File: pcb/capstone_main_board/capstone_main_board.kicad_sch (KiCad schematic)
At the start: 46 parts, among them J1 Vin, J10 MOSI, J11 SCLK, J12 NCS, J13 Vin, J18 SDO, J19 BAT, J2 VDD OS, J20 IO14, J21 IO13, J22 IO10, J23 IO8, J24 IO6, J25 RX0, J26 TX0, J27 D+, J28 D-, J29 100, J3 VDDA, J30 5V, J31 RESET, J32 Vin, J4 MFIO, J5 VDD FS, J6 V2, J7 V1, J8 Motion, J9 MISO, Q1 BSS138, Q2 BSS138, U1 OMGS3, U2 ADXL345, U3 TPS73219DBVT, U5 VREG_SOT23-5

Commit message: sensor and mcu board nearly complete
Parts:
- removed C2, C4: 1uF, Library:CAP_CL10_SAM, symbol Device:C
- removed C7: 10µF, Library:CAP_CL21_SAM, symbol Adafruit ADXL345 Triple-Axis Accelerometer-eagle-import:CAP_CERAMIC0805-NOOUTLI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
- removed C8: 0.1uF, Library:CAP_CL05_SAM, symbol Adafruit ADXL345 Triple-Axis Accelerometer-eagle-import:CAP_CERAMIC0805-NOOUTLI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
- removed D1: 1N4148, Library:SOD3715X135N, symbol Adafruit ADXL345 Triple-Axis Accelerometer-eagle-import:microbuilder_DIODE_SOD3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
- removed J1, J13, J32: Vin, Connector_PinHeader_1.00mm:PinHeader_1x01_P1.00mm_Vertical, symbol Connector:Conn_01x01_Pin
- removed J18: SDO, Connector_PinHeader_1.00mm:PinHeader_1x01_P1.00mm_Vertical, symbol Connector:Conn_01x01_Pin
- removed J2: VDD OS, Connector_PinHeader_1.00mm:PinHeader_1x01_P1.00mm_Vertical, symbol Connector:Conn_01x01_Pin
- removed J20: IO14, Connector_PinHeader_1.00mm:PinHeader_1x01_P1.00mm_Vertical, symbol Connector:Conn_01x01_Pin
- removed J21: IO13, Connector_PinHeader_1.00mm:PinHeader_1x01_P1.00mm_Vertical, symbol Connector:Conn_01x01_Pin
- removed J22: IO10, Connector_PinHeader_1.00mm:PinHeader_1x01_P1.00mm_Vertical, symbol Connector:Conn_01x01_Pin
- removed J23: IO8, Connector_PinHeader_1.00mm:PinHeader_1x01_P1.00mm_Vertical, symbol Connector:Conn_01x01_Pin
- removed J24: IO6, Connector_PinHeader_1.00mm:PinHeader_1x01_P1.00mm_Vertical, symbol Connector:Conn_01x01_Pin
- removed J25: RX0, Connector_PinHeader_1.00mm:PinHeader_1x01_P1.00mm_Vertical, symbol Connector:Conn_01x01_Pin
- removed J26: TX0, Connector_PinHeader_1.00mm:PinHeader_1x01_P1.00mm_Vertical, symbol Connector:Conn_01x01_Pin
- removed J27: D+, Connector_PinHeader_1.00mm:PinHeader_1x01_P1.00mm_Vertical, symbol Connector:Conn_01x01_Pin
- removed J28: D-, Connector_PinHeader_1.00mm:PinHeader_1x01_P1.00mm_Vertical, symbol Connector:Conn_01x01_Pin
- removed J29: 100, Connector_PinHeader_1.00mm:PinHeader_1x01_P1.00mm_Vertical, symbol Connector:Conn_01x01_Pin
- removed J30: 5V, Connector_PinHeader_1.00mm:PinHeader_1x01_P1.00mm_Vertical, symbol Connector:Conn_01x01_Pin
- removed J31: RESET, Connector_PinHeader_1.00mm:PinHeader_1x01_P1.00mm_Vertical, symbol Connector:Conn_01x01_Pin
- removed J5: VDD FS, Connector_PinHeader_1.00mm:PinHeader_1x01_P1.00mm_Vertical, symbol Connector:Conn_01x01_Pin
- removed Q1, Q2: BSS138, Library:SOT95P240X111-3N, symbol Adafruit ADXL345 Triple-Axis Accelerometer-eagle-import:MOSFET-NWIDE
- removed R4, R5, R6, R7: 10K, Library:RES_ERJ2RKF1002X, symbol Adafruit ADXL345 Triple-Axis Accelerometer-eagle-import:RESISTOR0805_NOOUTLINE
- removed U1: OMGS3, Library:OMGS3, symbol New_Library:OMGS3
- removed U2: ADXL345, Library:PQFN80P500X300X100-14N, symbol New_Library:ADXL345
- removed U3: TPS73219DBVT, Library:DBV5_TEX, symbol New_Library:TPS73219DBVT
- added C1: 10uF, Capacitor_SMD:C_0805_2012Metric, symbol Device:C
- added C3: 0.1uF, Capacitor_SMD:C_0402_1005Metric, symbol Device:C
- added C5: 1uF, Capacitor_SMD:C_0603_1608Metric, symbol Device:C
- added J7: VBAT-, Connector_PinHeader_2.00mm:PinHeader_1x01_P2.00mm_Vertical, symbol Connector:Conn_01x01_Pin
- added J8: Conn_01x07_Pin, Custom_FP:OMGS3_programming_pins, symbol Connector:Conn_01x07_Pin
- added R2: 10k, Resistor_SMD:R_0402_1005Metric, symbol Device:R
- added U1: OMGS3, Imported_FP:OMGS3, symbol Imported_sym:OMGS3
- added U3: ADXL345, Imported_FP:PQFN80P500X300X100-14N, symbol Imported_sym:ADXL345
- added U4: TPS73219DBVT, Imported_FP:DBV5_TEX, symbol Custom_sym:TPS73219DBVT
- C2: renamed from C1; footprint Library:CAP_CL10_SAM -> Capacitor_SMD:C_0603_1608Metric
- C4: renamed from C3; footprint Library:CAP_CL10_SAM -> Capacitor_SMD:C_0603_1608Metric
- J1: renamed from J4; footprint Connector_PinHeader_1.00mm:PinHeader_1x01_P1.00mm_Vertical -> Connector_PinHeader_2.00mm:PinHeader_1x01_P2.00mm_Vertical
- J10: renamed from J7; value V1 -> FORCE_V1; footprint Connector_PinHeader_1.00mm:PinHeader_1x01_P1.00mm_Vertical -> Connector_PinHeader_2.00mm:PinHeader_1x01_P2.00mm_Vertical
- J11: renamed from J19; value BAT -> VBAT+; footprint Connector_PinHeader_1.00mm:PinHeader_1x01_P1.00mm_Vertical -> Connector_PinHeader_2.00mm:PinHeader_1x01_P2.00mm_Vertical
- J12: renamed from J3; footprint Connector_PinHeader_1.00mm:PinHeader_1x01_P1.00mm_Vertical -> Connector_PinHeader_2.00mm:PinHeader_1x01_P2.00mm_Vertical
- J2: renamed from J8; footprint Connector_PinHeader_1.00mm:PinHeader_1x01_P1.00mm_Vertical -> Connector_PinHeader_2.00mm:PinHeader_1x01_P2.00mm_Vertical
- J3: renamed from J9; footprint Connector_PinHeader_1.00mm:PinHeader_1x01_P1.00mm_Vertical -> Connector_PinHeader_2.00mm:PinHeader_1x01_P2.00mm_Vertical
- J4: renamed from J10; footprint Connector_PinHeader_1.00mm:PinHeader_1x01_P1.00mm_Vertical -> Connector_PinHeader_2.00mm:PinHeader_1x01_P2.00mm_Vertical
- J5: renamed from J11; footprint Connector_PinHeader_1.00mm:PinHeader_1x01_P1.00mm_Vertical -> Connector_PinHeader_2.00mm:PinHeader_1x01_P2.00mm_Vertical
- J6: renamed from J12; footprint Connector_PinHeader_1.00mm:PinHeader_1x01_P1.00mm_Vertical -> Connector_PinHeader_2.00mm:PinHeader_1x01_P2.00mm_Vertical
- J9: renamed from J6; value V2 -> FORCE_V2; footprint Connector_PinHeader_1.00mm:PinHeader_1x01_P1.00mm_Vertical -> Connector_PinHeader_2.00mm:PinHeader_1x01_P2.00mm_Vertical
- R1: renamed from R8; footprint Library:RES_ERJ2RKF1002X -> Resistor_SMD:R_0402_1005Metric
- U2: renamed from U5; footprint Library:SOT95P285X140-5N -> Imported_FP:SOT95P280X145-5N
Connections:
- net +3.3V: now also C2.1, J8.7 (Pin_7), U1.16 (3V3), U4.1 (IN), U4.3 (EN); no longer C2.2, R1.2
- net GND: now also C2.2, C1.1, C3.1, C5.2, J7.1 (Pin_1), J8.1 (Pin_1), R2.2, U1.10 (GND), U3.2 (GND), U3.4 (GND), U3.5 (GND), U4.2 (GND); no longer C2.1
- net SCL: now also U1.23 (IO9), U3.14 (SCL/SCLK)
- net SDA/SDIO: now also U1.24 (IO8), U3.13 (SDA/SDI/SDIO)
- net ACCEL_VIN: now reaches U2.5 (OUT)
- net ACCEL_VIN: now also R1.2, C3.2, U3.1 (VDD_I/O), U3.6 (VS)
- net VBAT+: now reaches U2.1 (IN), U2.3 (EN)
- net VBAT+: now also J11.1 (Pin_1), C1.2, U1.17 (BAT)
- net at C4.1: now also U4.4 (NR/FB)
- net at J12.1 (Pin_1): now also C5.1, U4.5 (OUT)
- net at J1.1 (Pin_1): now also U1.8 (IO6)
- net at J3.1 (Pin_1): now also U1.6 (IO4)
- net at R1.1: now also U3.7 (~{CS})
- net at J9.1 (Pin_1): now also U1.20 (IO12)
- net at J10.1 (Pin_1): now also U1.21 (IO11)
- net at J6.1 (Pin_1): now also U1.3 (IO1)
- net at J5.1 (Pin_1): now also U1.4 (IO2)
- net at J4.1 (Pin_1): now also U1.5 (IO3)
- net at J2.1 (Pin_1): now also U1.7 (IO5)
- new net: J8.2 (Pin_2), U1.11 (RESET)
- new net: J8.3 (Pin_3), U1.12 (5V)
- new net: J8.4 (Pin_4), U1.13 (IO0)
- new net: J8.5 (Pin_5), U1.14 (D-)
- new net: J8.6 (Pin_6), U1.15 (D+)
- new net SDO/ADDR: R2.1, U1.25 (IO7), U3.12 (SDO/ALT_ADDRESS)
- no-connect marks 4 -> 12
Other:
- note added: "ADXL345 accelerometer"
- note added: "ADXL345 power"
- note added: "OMGS3 controller"
- note added: "PAW3040 sensor power"
- note removed: "VDDIO"
- moved on the sheet: C2, C4, J1, J10, J11, J12, J2, J3, J4, J5, J6, J9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

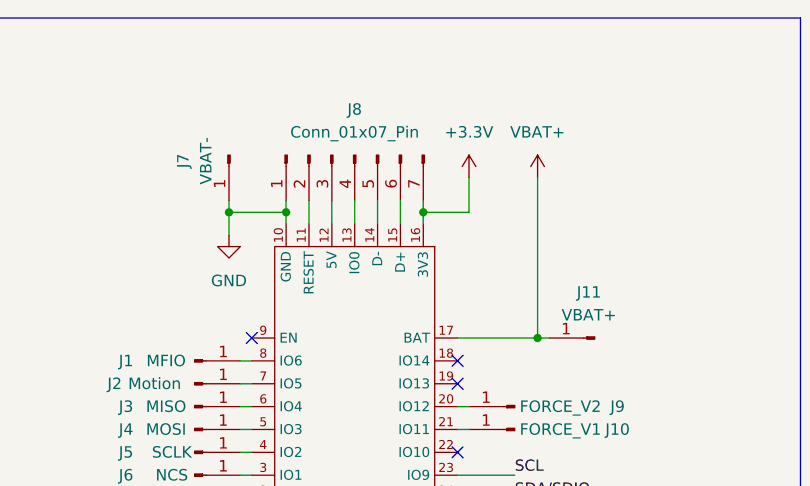
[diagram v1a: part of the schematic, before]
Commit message: added teardrops
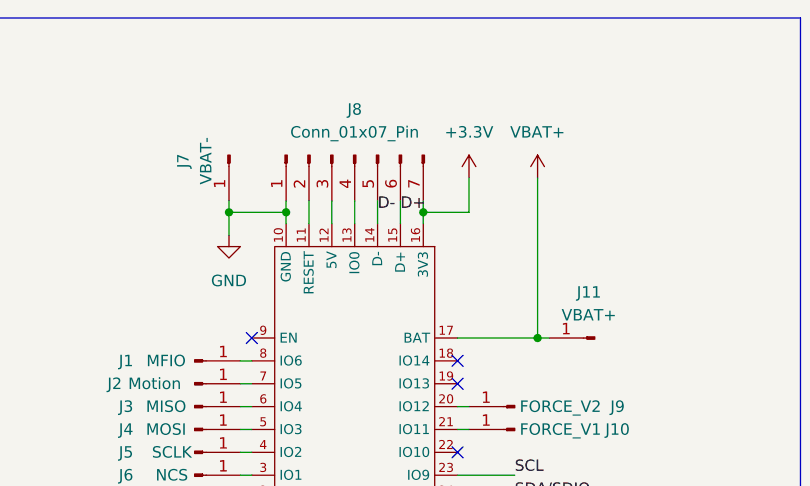
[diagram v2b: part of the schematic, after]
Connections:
- net D-: now reaches J8.5 (Pin_5), U1.14 (D-)
- net D+: now reaches J8.6 (Pin_6), U1.15 (D+)
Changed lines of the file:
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@@
+		)
+	)
+	(label "D-"
+		(at 72.39 41.91 0)
+		(effects
+			(font
+				(size 1.27 1.27)
+			)
+			(justify left bottom)
 		)
 	)
@@
 			)
 			(justify left bottom)
+		)
+	)
+	(label "D+"
+		(at 74.93 41.91 0)
+		(effects
+			(font
+				(size 1.27 1.27)
+			)
+			(justify left bottom)
